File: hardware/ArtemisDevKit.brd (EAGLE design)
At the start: 94 x 38.1 mm, 231 parts, among them J1 USB, J10 SMD, J11 SMD, J14 PTH, J2 CORTEX_JTAG_DEBUG_MINIMUM_PTH, J22 PTH, J23 PTH, J24 PTH, J25 PTH, J26 PTH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

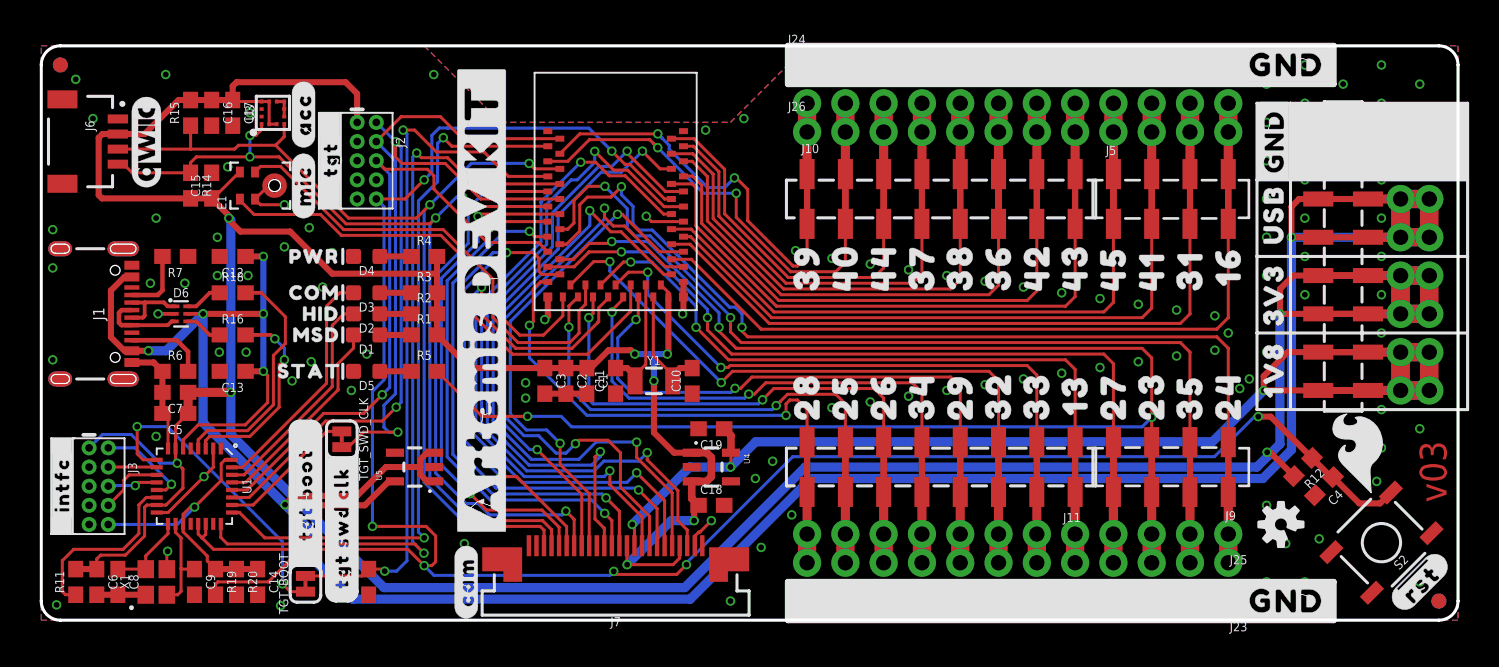
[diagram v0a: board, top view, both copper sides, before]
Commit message: shift USB-C connector down 50 mil
this is to make it properly centered on the board
purely aesthetic motivation, with copper changes
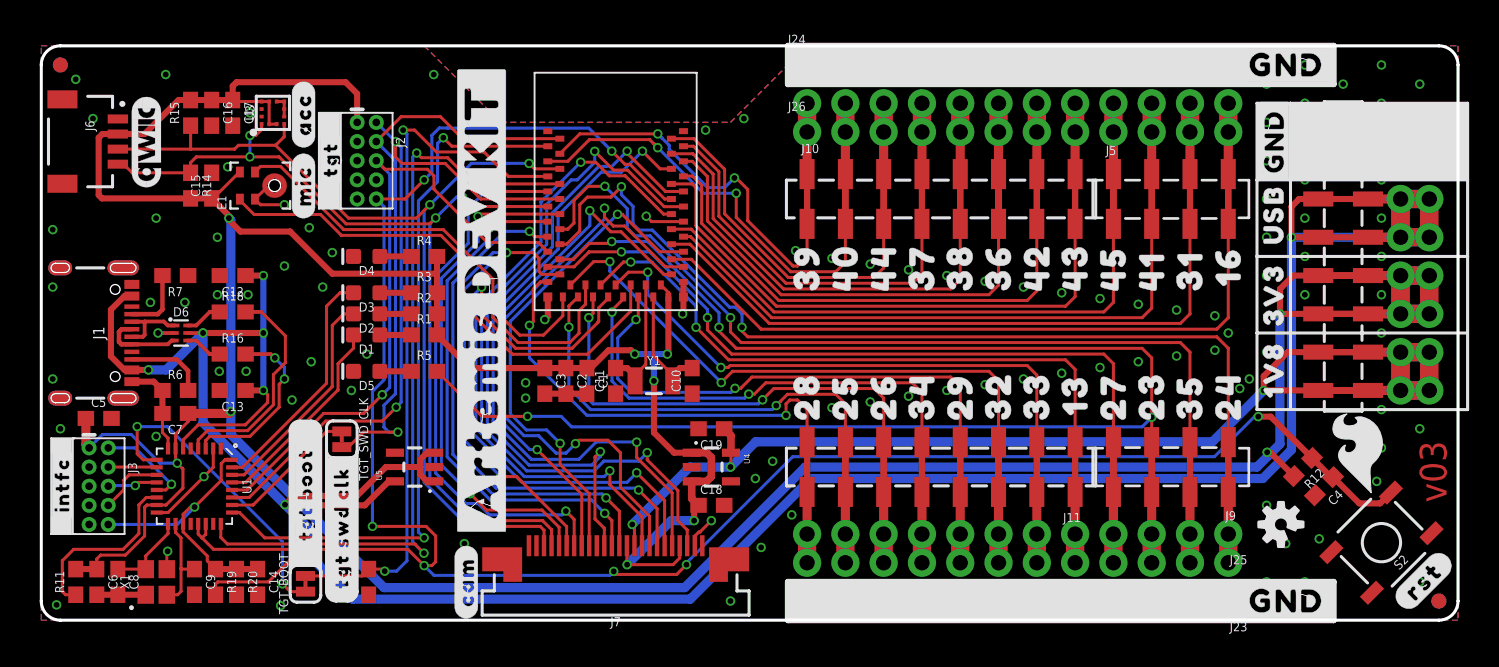
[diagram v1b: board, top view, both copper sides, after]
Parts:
- removed LOGO2: SFE_LOGO_NAME_FLAME.2_INCH, SparkFun-Aesthetics:SFE_LOGO_NAME_FLAME_.2
- removed U$117: (no value), buzzard_labels:6_PWR
- removed U$118: (no value), buzzard_labels:7_COM
- removed U$119: (no value), buzzard_labels:8_HID
- removed U$120: (no value), buzzard_labels:9_MSD
- removed U$121: (no value), buzzard_labels:10_STAT
- removed U$122: (no value), buzzard_labels:18_##RST##
- added U$142: (no value), buzzard_labels:13_#RST#
- added U$143: (no value), SparkFun-Aesthetics:SFE_LOGO_NAME_FLAME_.2
- J1: value USB -> (none)
- J10, J11: value SMD -> (none)
- J14, J22, J23, J24, J25, J26: value PTH -> (none)
- J5, J9: value SMD -> 1X04_SMD_STRAIGHT_COMBO
- moved C5 5.09 mm to (3.81, 13.4), turned to 0 degrees
- moved C7 1.40 mm to (8.89, 13.7)
- moved C13 1.27 mm to (12.7, 15.2)
- moved R6 1.27 mm to (8.89, 15.2)
- moved C12 1.27 mm to (12.7, 22.9)
- moved D6 1.27 mm to (9.27, 19.1)
- moved J1 1.27 mm to (6.35, 19.1)
- moved R16 1.27 mm to (12.7, 17.7)
- moved R18 1.27 mm to (12.7, 20.4)
- moved R7 1.27 mm to (8.89, 22.9)
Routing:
- net V_USB: track 196.5 -> 193.9 mm
- net GND: track 112.7 -> 111.5 mm, vias 108 -> 109
- net USB_D+_P: track 13.3 -> 12.0 mm
- net USB_D-_P: track 16.0 -> 14.7 mm
- net 3.3V: track 284.3 -> 285.0 mm

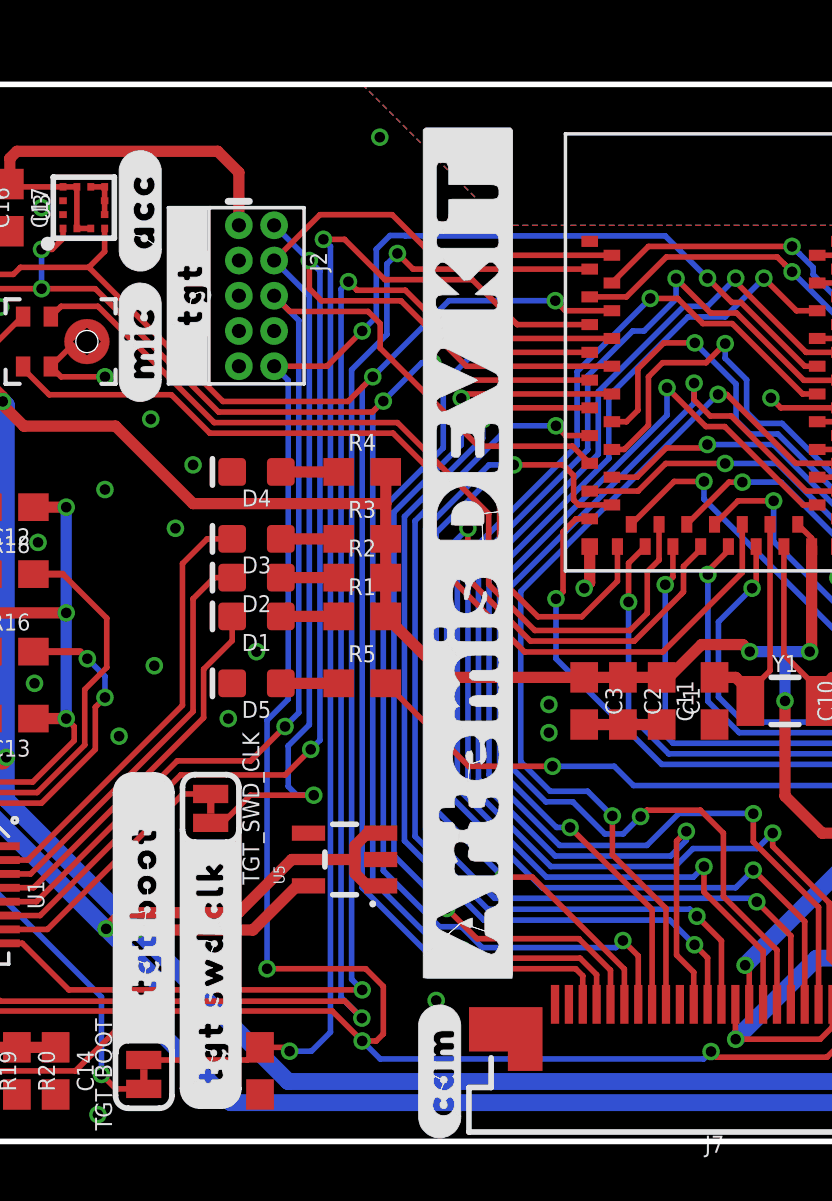
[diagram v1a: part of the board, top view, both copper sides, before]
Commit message: shift tgt swd connector
this centers the label between the labels for the mic and acc
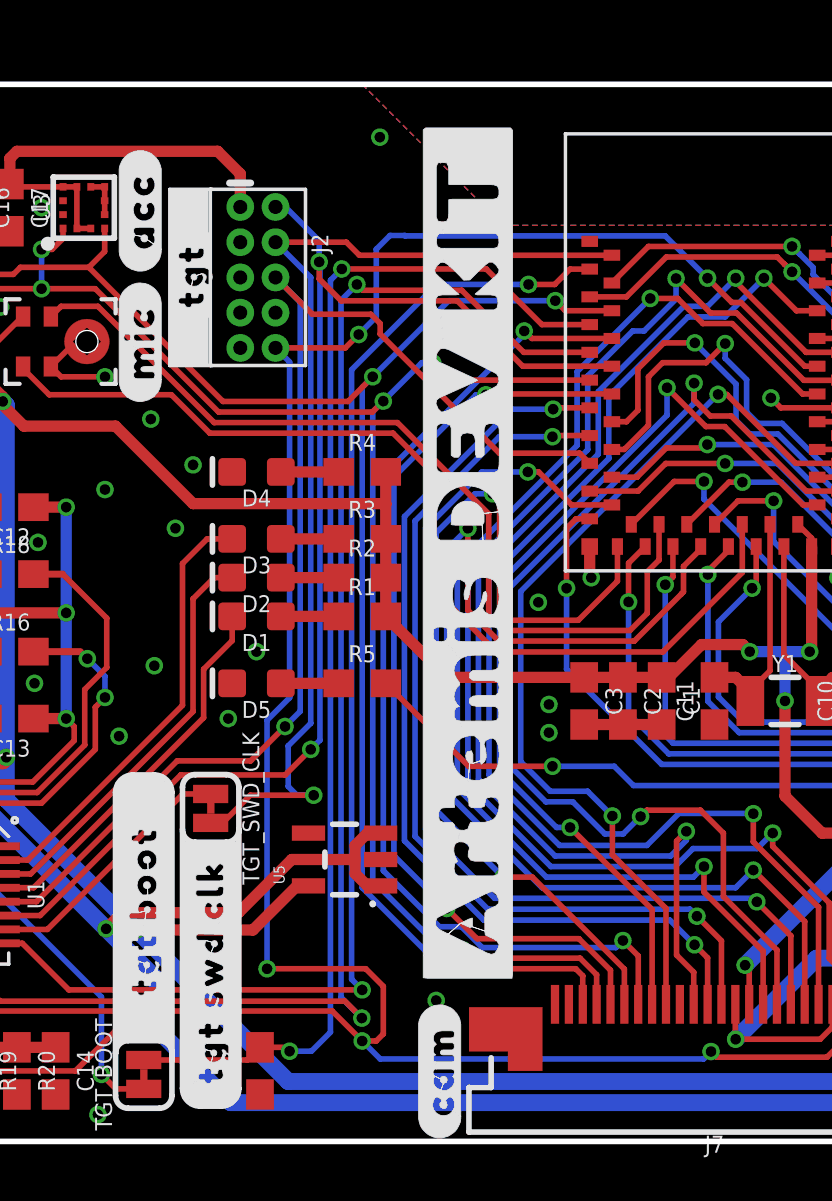
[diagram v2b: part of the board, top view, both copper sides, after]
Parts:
- moved J2 0.66 mm to (21.6, 31.1)
- moved U$136 0.66 mm to (19.2, 29.4)
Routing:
- net TGT_BOOT: track 46.8 -> 44.7 mm
- net TGT_RX: track 48.0 -> 46.0 mm
- net CAMERA_TRIG: track 36.8 -> 36.1 mm
- net CAMERA_VSYNC: track 41.3 -> 42.0 mm
- net PDM_CLK: track 31.6 -> 32.3 mm
- net 3.3V: track 285.0 -> 284.4 mm
- net TGT_SWO: track 43.1 -> 43.7 mm
- net PDM_DATA: track 35.0 -> 35.6 mm
- net CAMERA_INT: track 37.8 -> 37.2 mm
- net GND: track 111.5 -> 111.0 mm, vias 109 -> 110

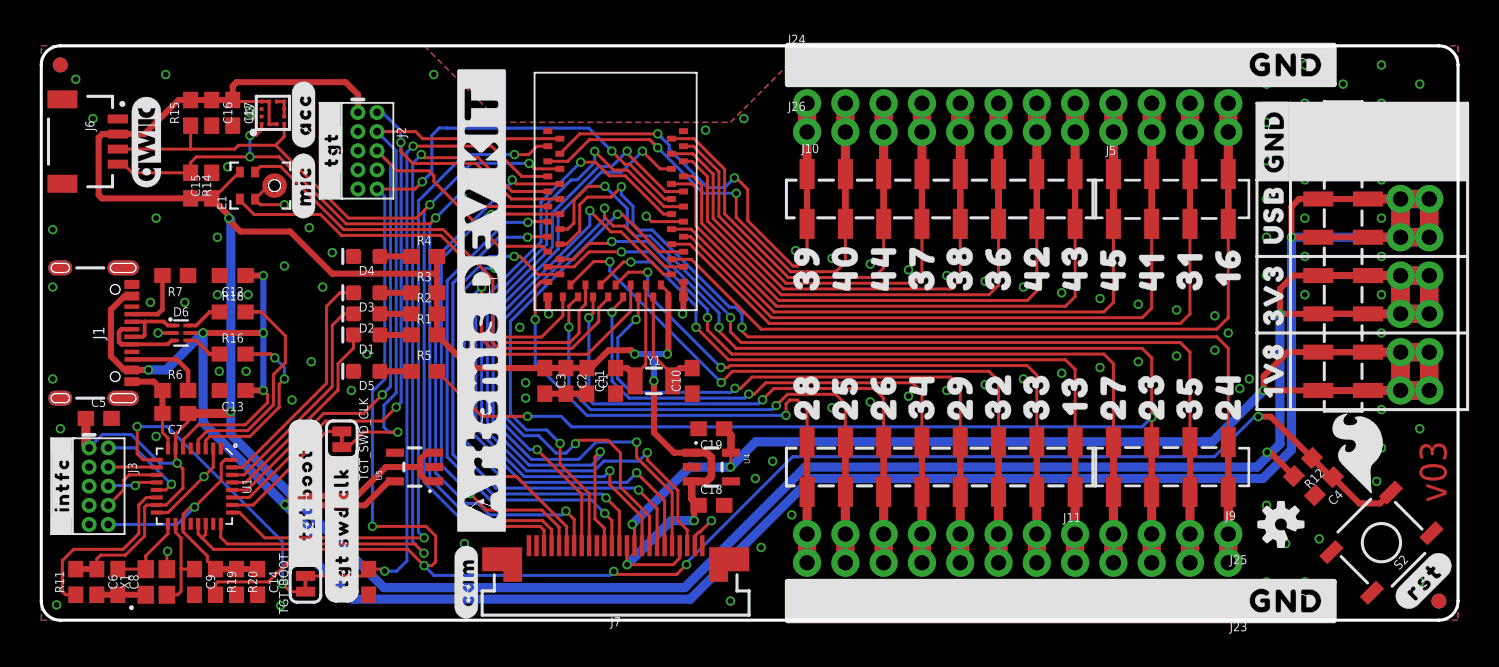
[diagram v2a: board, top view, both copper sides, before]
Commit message: address Pete's reviews
- improve GND pour on lower layer
- fix ERC errors (mismatched values, footprints)
- add LED buzzard labels
- fix version in copper and schematic
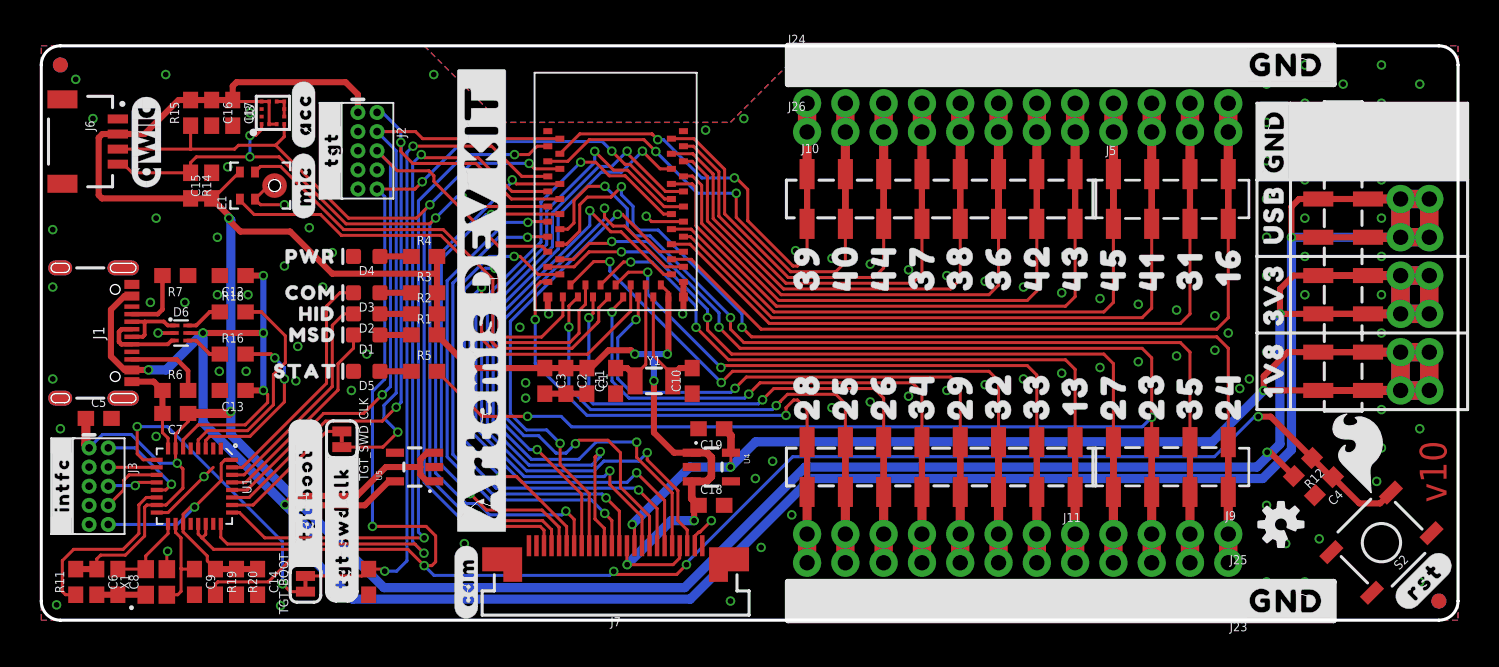
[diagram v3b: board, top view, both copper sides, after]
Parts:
- added U$117: (no value), buzzard_labels:7_COM
- added U$118: (no value), buzzard_labels:8_HID
- added U$119: (no value), buzzard_labels:9_MSD
- added U$120: (no value), buzzard_labels:10_STAT
- added U$121: (no value), buzzard_labels:6_PWR
- J1: value (none) -> USB
- J10, J11, J4: value (none) -> SMD
- J12, J14, J22, J23, J24, J25, J26, J8: value (none) -> PTH
- J5, J9: value 1X04_SMD_STRAIGHT_COMBO -> SMD
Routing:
- net !TGT_RST: track 144.0 -> 141.8 mm
- net GND: track 111.0 -> 109.8 mm
- net D39: track 32.9 -> 32.2 mm
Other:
- board text added: "v10"
- board text removed: "v03"

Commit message: update silkscreen
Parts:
- removed U$143: (no value), SparkFun-Aesthetics:SFE_LOGO_NAME_FLAME_.2
- added LOGO2: SFE_LOGO_NAME_FLAME.2_INCH, SparkFun-Aesthetics:SFE_LOGO_NAME_FLAME_.2
- J5, J9: value SMD -> 1X04_SMD_STRAIGHT_COMBO
- J7: device SparkFun-Connectors:FPC-24-AMPHENOL-SFV24R-1STE1HLF -> SparkFun-Connectors:FPC05024-42201
- U$111: device buzzard_labels:1_#ARTEMIS_DEV_KIT# -> buzzard_labels:#SDA#SDI#24
- U$112: device buzzard_labels:0_#ARTEMIS_DEV_KIT# -> buzzard_labels:#SDO#25
- U$35: device buzzard_labels:22_#SCL#SCLK# -> buzzard_labels:ARTEMIS_DEV_KIT0
- U$36: device buzzard_labels:23_#SDA#MISO# -> buzzard_labels:ARTEMIS_DEV_KIT1
- U$37: device buzzard_labels:24_#MOSI# -> buzzard_labels:#SCL#SCK#23
- moved FD1 91.4 mm to (92.7, 36.8), flipped to the bottom
- moved FD2 91.4 mm to (92.7, 36.8), flipped to the top
- moved FD3 91.4 mm to (1.27, 1.27), flipped to the bottom
- moved FD4 91.4 mm to (1.27, 1.27), flipped to the top
- moved U$135 91.2 mm to (92.6, 6.48), flipped to the bottom
- moved U$113 90.5 mm to (92.2, 30.7), flipped to the top
- moved J8 90.2 mm to (1.91, 33.0), flipped to the bottom
- moved U$115 89.5 mm to (91.8, 36.1), flipped to the top
- moved R11 89.4 mm to (91.7, 2.54), flipped to the bottom
- moved C6 86.6 mm to (90.3, 2.54), flipped to the bottom
- moved C5 86.4 mm to (90.2, 13.4), flipped to the bottom
- moved J12 86.4 mm to (3.81, 33.0), flipped to the bottom
- moved J3 86.4 mm to (90.2, 8.89), flipped to the bottom
- moved U$142 86.2 mm to (3.87, 1.02), flipped to the bottom
- moved C8 83.8 mm to (88.9, 2.54), flipped to the bottom
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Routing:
- net GND: track 109.8 -> 113.0 mm
- net CAMERA_PCLK: track 34.5 -> 36.5 mm
- net SDA: track 65.1 -> 67.1 mm
- net CAMERA_TRIG: track 36.1 -> 38.1 mm
- net CAMERA_INT: track 37.2 -> 39.2 mm
- net 1.8V: track 87.3 -> 89.3 mm
- net CAMERA_VSYNC: track 42.0 -> 44.0 mm
- net CAMERA_HSYNC: track 33.3 -> 35.3 mm
- net CAMERA_D6: track 33.6 -> 35.6 mm
- net CAMERA_D5: track 33.5 -> 35.5 mm
- net CAMERA_D3: track 44.1 -> 46.1 mm
- net CAMERA_D2: track 44.2 -> 46.2 mm
- net CAMERA_D1: track 48.7 -> 50.7 mm
- net CAMERA_MCLK: track 40.1 -> 42.1 mm
- net CAMERA_D7: track 34.3 -> 36.3 mm
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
